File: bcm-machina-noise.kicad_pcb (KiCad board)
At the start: 2 copper layers, 0 parts

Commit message: starting layout
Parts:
- added C1: 100nF, Capacitor_THT:C_Rect_L7.0mm_W3.5mm_P5.00mm, F.Cu at (147.3, 81.4)
- added C2: 100nF, Capacitor_THT:C_Rect_L7.0mm_W3.5mm_P5.00mm, F.Cu at (154.9, 81.3)
- added C3: 100nF, Capacitor_THT:C_Rect_L7.0mm_W3.5mm_P5.00mm, F.Cu at (81.4, 68.6)
- added C4: C_Polarized, Capacitor_THT:CP_Radial_D5.0mm_P2.00mm, F.Cu at (94.0, 83.8)
- added C5: C_Polarized, Capacitor_THT:CP_Radial_D5.0mm_P2.00mm, F.Cu at (182.9, 109.2)
- added C6: 100nF, Capacitor_THT:C_Rect_L7.0mm_W3.5mm_P5.00mm, F.Cu at (61.0, 106.7)
- added C7: 100nF, Capacitor_THT:C_Rect_L7.0mm_W3.5mm_P5.00mm, F.Cu at (137.2, 66.1)
- added D1: LED, LED_THT:LED_D5.0mm, F.Cu at (91.4, 99.1)
- added D2: LED, LED_THT:LED_D5.0mm, F.Cu at (73.7, 99.1)
- added H1: NotePad, MountingHole:MountingHole_4.3mm_M4_DIN965_Pad, F.Cu at (73.7, 142.2)
- added H10: NotePad, MountingHole:MountingHole_4.3mm_M4_DIN965_Pad, F.Cu at (165.1, 142.2)
- added H11: NotePad, MountingHole:MountingHole_4.3mm_M4_DIN965_Pad, F.Cu at (175.3, 142.2)
- added H12: NotePad, MountingHole:MountingHole_4.3mm_M4_DIN965_Pad, F.Cu at (185.4, 142.2)
- added H2: NotePad, MountingHole:MountingHole_4.3mm_M4_DIN965_Pad, F.Cu at (83.8, 142.2)
- added H3: NotePad, MountingHole:MountingHole_4.3mm_M4_DIN965_Pad, F.Cu at (94.0, 142.2)
- added H4: NotePad, MountingHole:MountingHole_4.3mm_M4_DIN965_Pad, F.Cu at (104.1, 142.2)
- added H5: NotePad, MountingHole:MountingHole_4.3mm_M4_DIN965_Pad, F.Cu at (114.3, 142.2)
- added H6: NotePad, MountingHole:MountingHole_4.3mm_M4_DIN965_Pad, F.Cu at (124.5, 142.2)
- added H7: NotePad, MountingHole:MountingHole_4.3mm_M4_DIN965_Pad, F.Cu at (134.6, 142.2)
- added H8: NotePad, MountingHole:MountingHole_4.3mm_M4_DIN965_Pad, F.Cu at (144.8, 142.2)
- added H9: NotePad, MountingHole:MountingHole_4.3mm_M4_DIN965_Pad, F.Cu at (154.9, 142.2)
- added J1: USB_A, USBPower:AMPHENOL_10103593-0001LF, F.Cu at (56.4, 69.3)
- added J2: AVR-ISP-6, Connector_PinHeader_2.54mm:PinHeader_2x03_P2.54mm_Vertical, F.Cu at (99.1, 71.1)
- added J3: AudioJack2_SwitchT, Connector_Audio:Jack_3.5mm_QingPu_WQP-PJ398SM_Vertical_CircularHoles, F.Cu at (182.9, 90.7)
- added J5: AudioJack2_SwitchT, Connector_Audio:Jack_3.5mm_QingPu_WQP-PJ398SM_Vertical_CircularHoles, F.Cu at (50.8, 123.2)
- added Q1: 2N5457, Package_TO_SOT_THT:TO-92L_Inline_Wide, F.Cu at (147.3, 76.2)
- added Q2: 2N5457, Package_TO_SOT_THT:TO-92L_Inline_Wide, F.Cu at (154.9, 76.2)
- added R1: 10k, Resistor_THT:R_Axial_DIN0207_L6.3mm_D2.5mm_P10.16mm_Horizontal, F.Cu at (73.7, 134.6)
- added R10: 10k, Resistor_THT:R_Axial_DIN0207_L6.3mm_D2.5mm_P10.16mm_Horizontal, F.Cu at (165.1, 134.6)
- added R11: 10k, Resistor_THT:R_Axial_DIN0207_L6.3mm_D2.5mm_P10.16mm_Horizontal, F.Cu at (175.3, 134.6)
- added R12: 10k, Resistor_THT:R_Axial_DIN0207_L6.3mm_D2.5mm_P10.16mm_Horizontal, F.Cu at (185.4, 134.6)
- added R13: 10k, Resistor_THT:R_Axial_DIN0207_L6.3mm_D2.5mm_P10.16mm_Horizontal, F.Cu at (104.1, 78.7)
- added R14: 10k, Resistor_THT:R_Axial_DIN0207_L6.3mm_D2.5mm_P10.16mm_Horizontal, F.Cu at (137.2, 76.2)
- added R15: 10k, Resistor_THT:R_Axial_DIN0207_L6.3mm_D2.5mm_P10.16mm_Horizontal, F.Cu at (129.5, 99.1)
- added R16: 10k, Resistor_THT:R_Axial_DIN0207_L6.3mm_D2.5mm_P10.16mm_Horizontal, F.Cu at (162.6, 88.9)
- added R17: 10k, Resistor_THT:R_Axial_DIN0207_L6.3mm_D2.5mm_P10.16mm_Horizontal, F.Cu at (167.6, 99.1)
- added R18: 10k, Resistor_THT:R_Axial_DIN0207_L6.3mm_D2.5mm_P10.16mm_Horizontal, F.Cu at (66.0, 86.4)
- added R19: 100k, Resistor_THT:R_Axial_DIN0207_L6.3mm_D2.5mm_P10.16mm_Horizontal, F.Cu at (66.0, 81.3)
- added R2: 10k, Resistor_THT:R_Axial_DIN0207_L6.3mm_D2.5mm_P10.16mm_Horizontal, F.Cu at (83.8, 134.6)
- added R20: 1k, Resistor_THT:R_Axial_DIN0207_L6.3mm_D2.5mm_P10.16mm_Horizontal, F.Cu at (86.4, 104.1)
- added R21: 1k, Resistor_THT:R_Axial_DIN0207_L6.3mm_D2.5mm_P10.16mm_Horizontal, F.Cu at (81.3, 104.1)
- added R22: 100k, Resistor_THT:R_Axial_DIN0207_L6.3mm_D2.5mm_P10.16mm_Horizontal, F.Cu at (45.7, 116.8)
- added R25: 10k, Resistor_THT:R_Axial_DIN0207_L6.3mm_D2.5mm_P10.16mm_Horizontal, F.Cu at (55.9, 96.5)
- added R26: 10k, Resistor_THT:R_Axial_DIN0207_L6.3mm_D2.5mm_P10.16mm_Horizontal, F.Cu at (50.8, 96.5)
- added R3: 10k, Resistor_THT:R_Axial_DIN0207_L6.3mm_D2.5mm_P10.16mm_Horizontal, F.Cu at (94.0, 134.6)
- added R4: 10k, Resistor_THT:R_Axial_DIN0207_L6.3mm_D2.5mm_P10.16mm_Horizontal, F.Cu at (104.1, 134.6)
- added R5: 10k, Resistor_THT:R_Axial_DIN0207_L6.3mm_D2.5mm_P10.16mm_Horizontal, F.Cu at (114.3, 134.6)
- added R6: 10k, Resistor_THT:R_Axial_DIN0207_L6.3mm_D2.5mm_P10.16mm_Horizontal, F.Cu at (124.5, 134.6)
- added R7: 10k, Resistor_THT:R_Axial_DIN0207_L6.3mm_D2.5mm_P10.16mm_Horizontal, F.Cu at (134.6, 134.6)
- added R8: 10k, Resistor_THT:R_Axial_DIN0207_L6.3mm_D2.5mm_P10.16mm_Horizontal, F.Cu at (144.8, 134.6)
- added R9: 10k, Resistor_THT:R_Axial_DIN0207_L6.3mm_D2.5mm_P10.16mm_Horizontal, F.Cu at (154.9, 134.6)
- added RV1: 10kA, Potentiometer_THT:Potentiometer_Alpha_RD902F-40-00D_Dual_Vertical, F.Cu at (149.9, 104.3)
- added RV2: 100k, Potentiometer_THT:Potentiometer_Alpha_RD901F-40-00D_Single_Vertical, F.Cu at (167.6, 104.3)
- added RV3: 10k, Trimpot:Potentiometer_THT_Bourns_3306P_Vertical, F.Cu at (124.5, 80.0)
- added RV4: 100k, Potentiometer_THT:Potentiometer_Alpha_RD901F-40-00D_Single_Vertical, F.Cu at (132.1, 104.3)
- added RV5: 100k, Potentiometer_THT:Potentiometer_Alpha_RD901F-40-00D_Single_Vertical_CircularHoles, F.Cu at (114.3, 104.3)
- added SW1: SW_Push, Button_Switch_THT:SW_PUSH_6mm, F.Cu at (72.4, 109.5)
- added SW2: SW_Push, Button_Switch_THT:SW_PUSH_6mm, F.Cu at (89.5, 109.8)
- added U1: 4069, Package_DIP:DIP-14_W7.62mm, F.Cu at (142.3, 71.1)
- added U2: MCP602, Package_DIP:DIP-8_W7.62mm, F.Cu at (55.9, 100.3)
- added U3: ATtiny84V-10P, Package_DIP:DIP-14_W7.62mm, F.Cu at (80.0, 73.7)
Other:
- board outline added: 11 x 6.1 mm

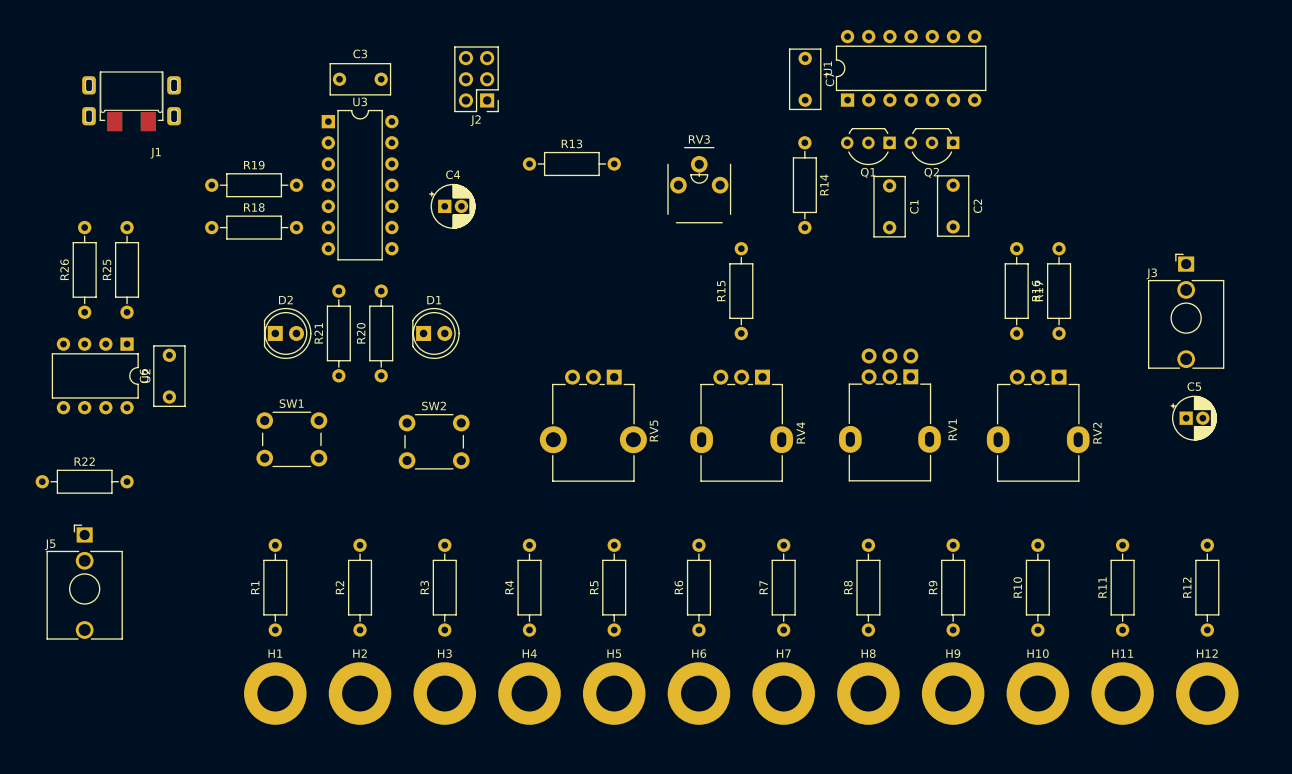
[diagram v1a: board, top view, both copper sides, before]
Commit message: USB traces fixed
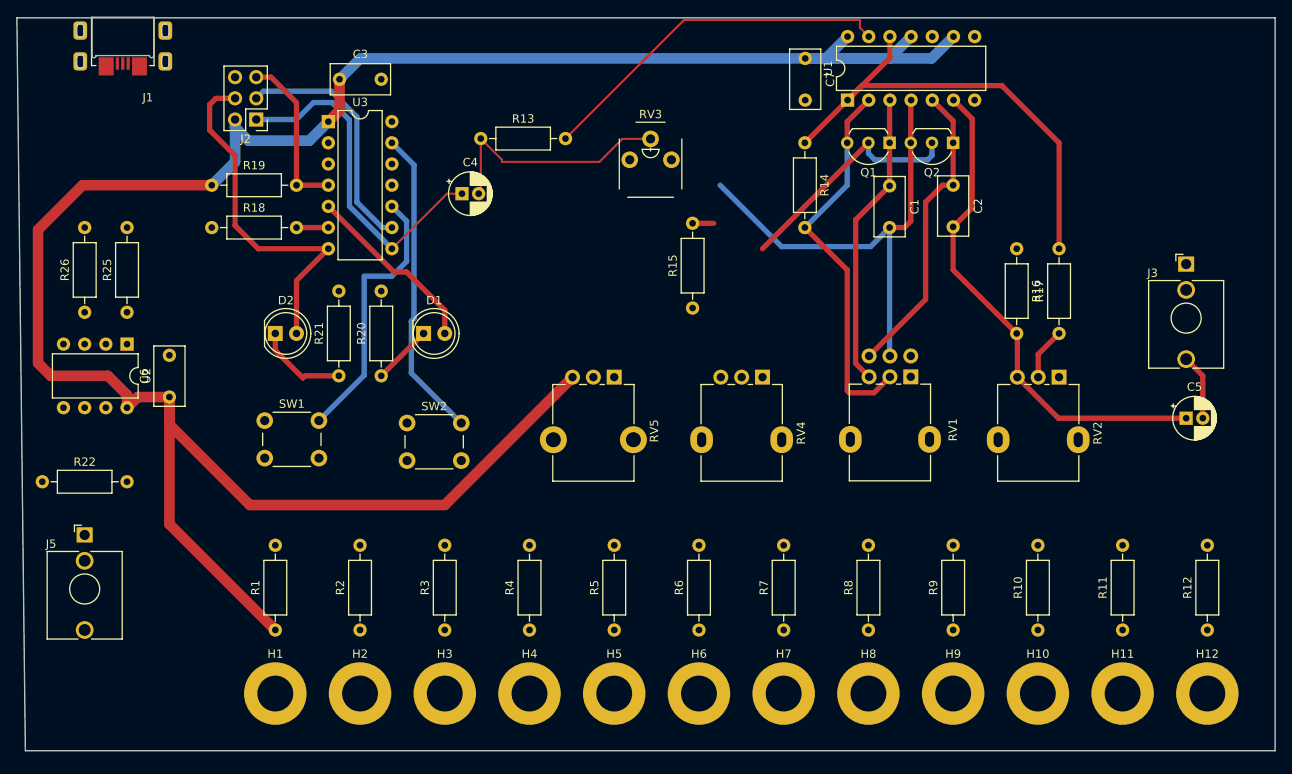
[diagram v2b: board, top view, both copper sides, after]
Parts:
- moved J2 27.8 mm to (71.4, 73.4)
- moved J1 6.66 mm to (55.4, 62.7)
- moved R13 6.59 mm to (98.3, 75.7)
- moved R15 6.59 mm to (123.7, 96.0)
- moved RV3 6.59 mm to (118.7, 77.0)
- moved C4 2.57 mm to (96.0, 82.3)
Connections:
- C4 pad 1: /MCU_PWM_1 -> /MCU_MISO
- J2 pad 1: /MCU_DOUT2 -> /MCU_MISO
- U3 pad 10: unconnected-(U3-PA3-Pad10) -> /MCU_DIN2
- U3 pad 13: unconnected-(U3-AREF/PA0-Pad13) -> /MCU_DIN1
- U3 pad 2: /MCU_DIN1 -> unconnected-(U3-XTAL1/PB0-Pad2)
- U3 pad 3: /MCU_DIN2 -> unconnected-(U3-XTAL2/PB1-Pad3)
- U3 pad 5: /MCU_PWM_1 -> /MCU_DOUT2
- U3 pad 8: /MCU_DOUT2 -> /MCU_MISO
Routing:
- net VCC: track 0.00 -> 277.7 mm
- net Net-(C2-Pad2): track 0.00 -> 60.6 mm
- net Net-(R14-Pad1): track 0.00 -> 58.6 mm
- net Net-(Q2-S): track 0.00 -> 57.1 mm
- net Net-(Q1-S): track 0.00 -> 46.1 mm
- net Net-(R13-Pad2): track 0.00 -> 43.6 mm
- net /MCU_DOUT1: track 0.00 -> 43.2 mm
- net /MCU_MISO: track 0.00 -> 41.6 mm
- net /MCU_DIN1: track 0.00 -> 37.3 mm
- net Net-(Q2-D): track 0.00 -> 36.6 mm
- net Net-(Q1-D): track 0.00 -> 35.5 mm
- net /MCU_DIN2: track 0.00 -> 32.7 mm
- net Net-(Q1-G): track 0.00 -> 31.4 mm
- net Net-(C4-Pad2): track 0.00 -> 29.5 mm
- net /MCU_SCK: track 0.00 -> 29.4 mm
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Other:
- board size 11 x 6.1 mm -> 150.9 x 87.9 mm

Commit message: adapted layout for smaller PCB
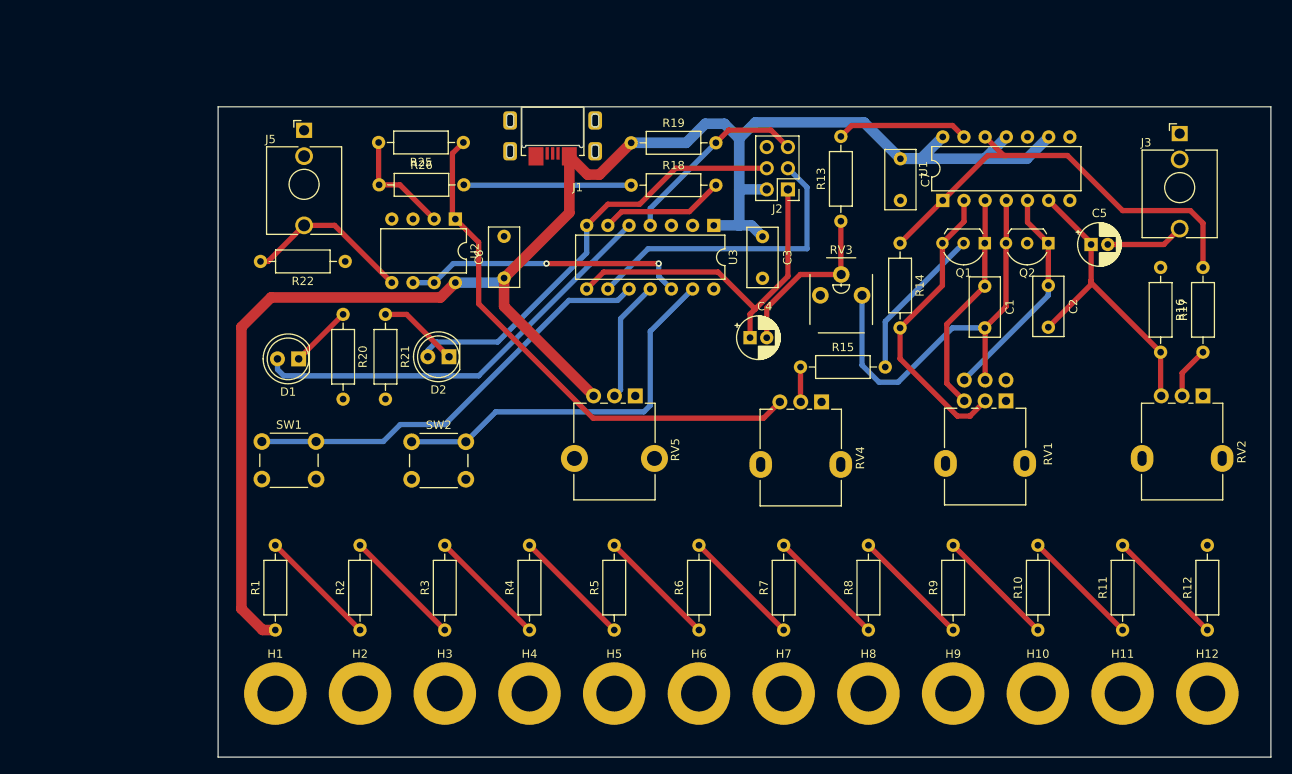
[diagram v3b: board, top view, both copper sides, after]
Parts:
- moved J2 64.3 mm to (135.1, 81.8)
- moved J5 55.2 mm to (77.1, 74.7)
- moved C3 54.1 mm to (132.1, 87.4), turned to -90 degrees
- moved J1 52.7 mm to (106.9, 73.5)
- moved R18 50.5 mm to (116.3, 81.3)
- moved R19 50.5 mm to (116.3, 76.2)
- moved U3 47.9 mm to (126.2, 86.1), turned to -90 degrees
- moved R25 45.2 mm to (96.2, 76.2), turned to 180 degrees
- moved R22 44.9 mm to (82.0, 90.4), turned to 180 degrees
- moved R13 44.3 mm to (141.5, 85.6), turned to 90 degrees
- moved C6 42.6 mm to (101.1, 92.4)
- moved U2 42.1 mm to (95.2, 85.3)
- moved C4 38.6 mm to (130.6, 99.6)
- moved R26 38.5 mm to (86.1, 81.2), turned to 0 degrees
- moved RV3 28.1 mm to (141.5, 93.2)
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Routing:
- net VCC: track 277.7 -> 204.6 mm
- net Net-(R25-Pad1): track 0.00 -> 63.8 mm
- net /MCU_ADC_1: track 0.00 -> 34.1 mm, vias 0 -> 2
- net /MCU_DOUT2: track 21.9 -> 51.2 mm
- net Net-(R13-Pad2): track 43.6 -> 15.9 mm
- net Net-(C2-Pad2): track 60.6 -> 36.8 mm
- net Net-(U2B-+): track 0.00 -> 20.4 mm
- net Net-(R18-Pad1): track 0.00 -> 20.1 mm
- net /MCU_DIN2: track 32.7 -> 51.6 mm
- net /MCU_ADC_2: track 0.00 -> 14.6 mm
- net Net-(H7-Pad1): track 0.00 -> 14.4 mm
- net Net-(H3-Pad1): track 0.00 -> 14.4 mm
- net Net-(H9-Pad1): track 0.00 -> 14.4 mm
- net Net-(H8-Pad1): track 0.00 -> 14.4 mm
- net Net-(H6-Pad1): track 0.00 -> 14.4 mm
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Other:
- board size 150.9 x 87.9 mm -> 126.2 x 78 mm

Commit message: traces tidied up with more space for ground plane
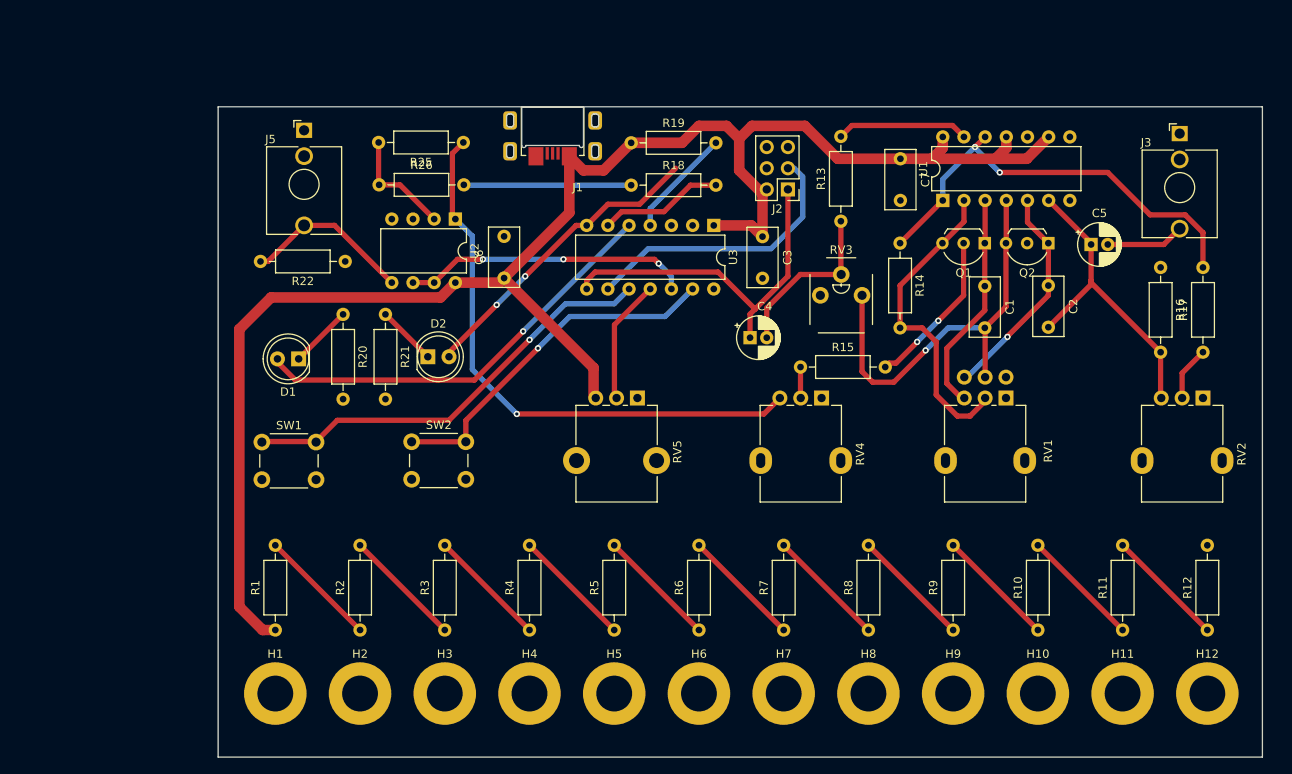
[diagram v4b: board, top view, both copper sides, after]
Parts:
- moved D2 2.54 mm to (91.9, 101.9), turned to 0 degrees
- moved RV4 0.47 mm to (139.2, 106.8)
- moved RV5 0.36 mm to (117.1, 106.8)
- moved RV1 0.35 mm to (161.3, 106.8)
- moved RV2 0.25 mm to (184.9, 106.8)
- moved SW1 0.07 mm to (72.0, 112.1)
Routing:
- net /MCU_DOUT1: track 52.4 -> 36.8 mm, vias 0 -> 2
- net /MCU_RESET: track 23.3 -> 13.2 mm
- net Net-(R25-Pad1): track 63.8 -> 68.6 mm, vias 0 -> 1
- net VCC: track 204.6 -> 200.2 mm
- net /MCU_DIN1: track 46.5 -> 42.8 mm, vias 0 -> 1
- net Net-(D2-K): track 9.72 -> 7.18 mm
- net /MCU_SCK: track 36.5 -> 34.0 mm
- net Net-(Q1-S): track 36.0 -> 37.5 mm
- net /MCU_MISO: track 42.5 -> 43.1 mm
- net Net-(Q1-G): track 18.7 -> 19.2 mm, vias 0 -> 2
- net Net-(Q2-S): track 49.3 -> 49.7 mm, vias 0 -> 1
- net /MCU_ADC_1: track 34.1 -> 34.5 mm, vias 2 -> 3
- net /MCU_DOUT2: track 51.2 -> 51.1 mm, vias 0 -> 1
- net Net-(R14-Pad1): track 52.8 -> 52.9 mm, vias 0 -> 2
- net Net-(Q2-D): track 26.7 -> 26.8 mm, vias 0 -> 1
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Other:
- board size 126.2 x 78 mm -> 125.2 x 78 mm

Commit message: Finalising traces and ground plane, all errors removed
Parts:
- moved J1 0.14 mm to (106.9, 73.7)
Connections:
- J1 pad 4: GND -> unconnected-(J1-GND-Pad4)
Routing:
- net /MCU_RESET: track 13.2 -> 29.1 mm
- net Net-(Q2-S): track 49.7 -> 38.5 mm, vias 1 -> 0
- net /MCU_DOUT1: track 36.8 -> 47.3 mm, vias 2 -> 0
- net VCC: track 200.2 -> 210.0 mm
- net Net-(Q1-G): track 19.2 -> 28.7 mm, vias 2 -> 0
- net Net-(H9-Pad1): track 14.4 -> 22.0 mm
- net Net-(H8-Pad1): track 14.4 -> 22.0 mm
- net Net-(H7-Pad1): track 14.4 -> 22.0 mm
- net Net-(H6-Pad1): track 14.4 -> 22.0 mm
- net Net-(H5-Pad1): track 14.4 -> 22.0 mm
- net Net-(H4-Pad1): track 14.4 -> 22.0 mm
- net Net-(H3-Pad1): track 14.4 -> 22.0 mm
- net Net-(H2-Pad1): track 14.4 -> 22.0 mm
- net Net-(H12-Pad1): track 14.4 -> 22.0 mm
- net Net-(H11-Pad1): track 14.4 -> 22.0 mm
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- added copper zone on B.Cu, net GND
- added copper zone on F.Cu, net GND
